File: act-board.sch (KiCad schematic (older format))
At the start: 15 parts, among them P1 B6B-PH-K-S(LF)(SN), P2 S2B-PH-K-S(LF)(SN), Q1 PN2222A, Q2 IRLB8721PBF, Q3 PN2222A, Q4 PN2222A

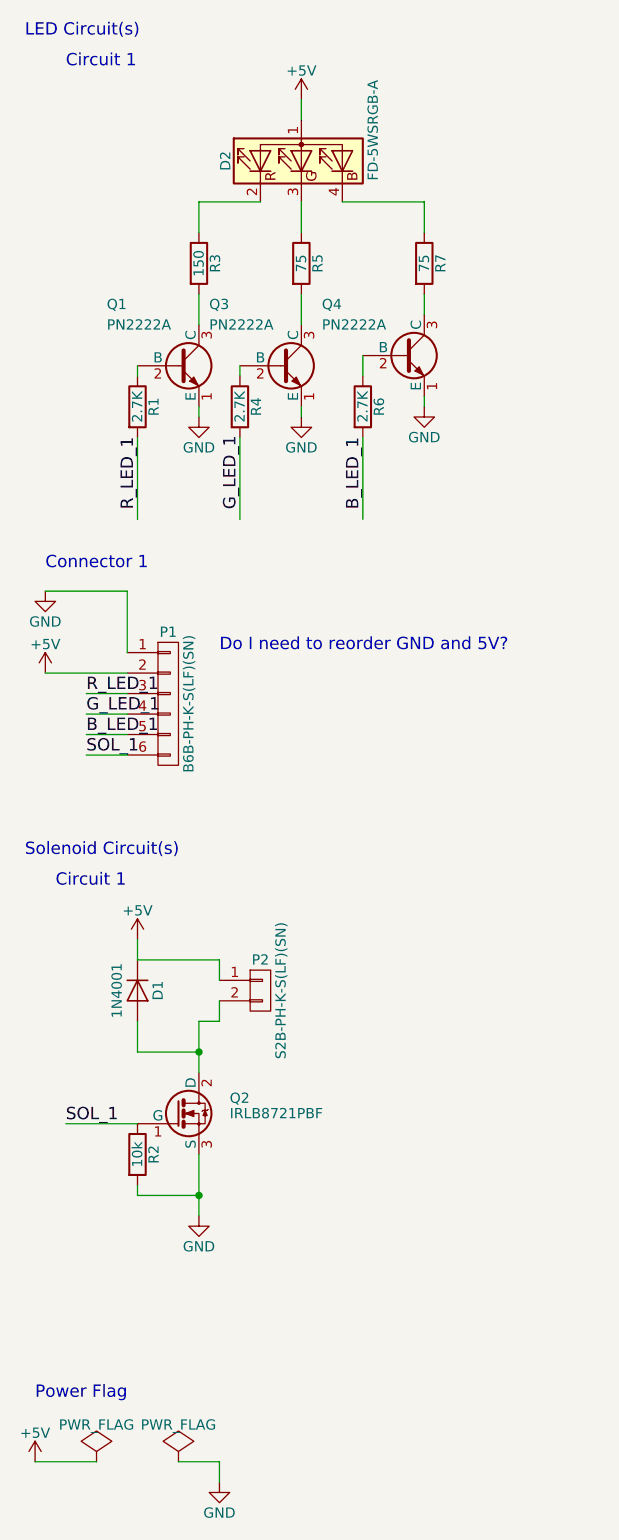
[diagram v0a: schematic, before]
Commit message: Fix RGB LED pad.
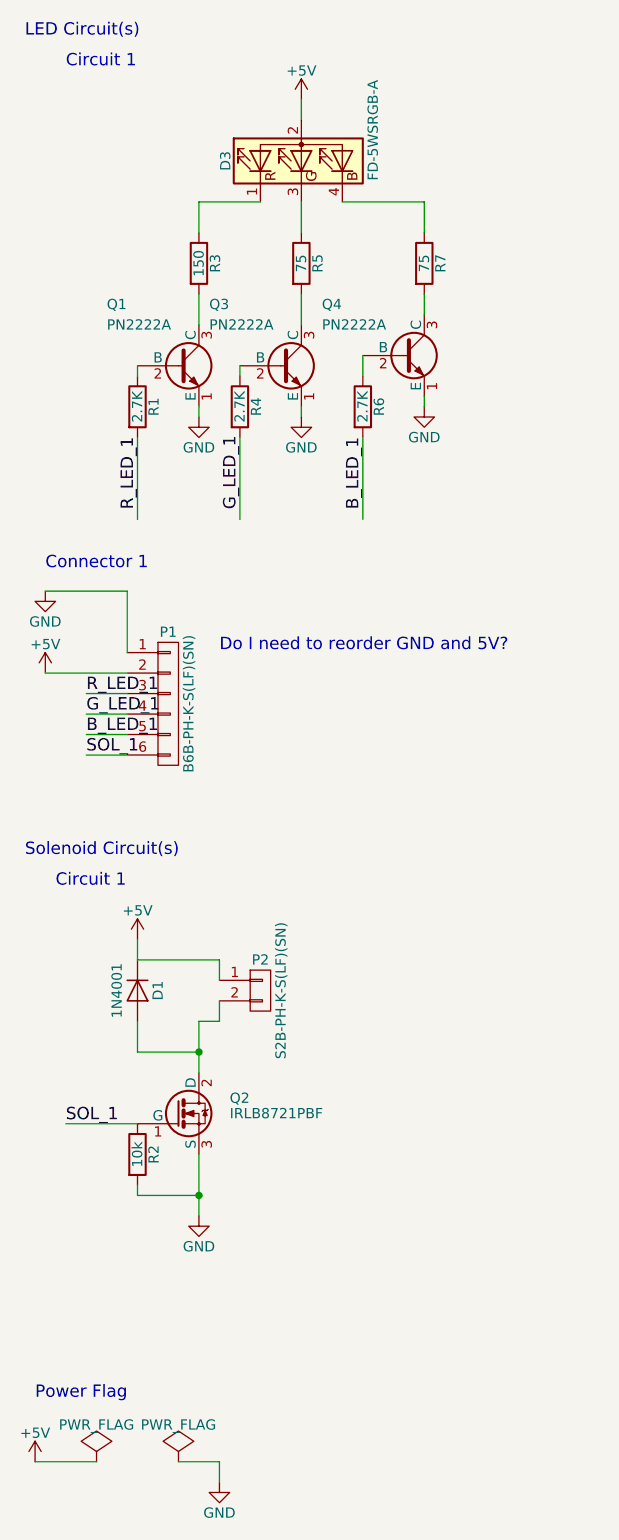
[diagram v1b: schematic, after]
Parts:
- removed D2: FD-5WSRGB-A, LEDs:LED-RGB-5MM_Common_Cathode, symbol LED_ARGB
- added D3: FD-5WSRGB-A, LEDs:LED_D5.0mm-4, symbol LED_RAGB
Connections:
- wire segments 40 -> 42
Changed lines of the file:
@@
 $EndDescr
-$Comp
-L LED_ARGB D2
-U 1 1 5865AF3E
-P 1900 1250
-F 0 "D2" H 1900 1620 50  0000 C CNN
-F 1 "FD-5WSRGB-A" H 2050 900 50  0000 C CNN
-F 2 "LEDs:LED-RGB-5MM_Common_Cathode" H 1900 1200 50  0001 C CNN
-F 3 "" H 1900 1200 50  0000 C CNN
-	1    1900 1250
-	0    -1   -1   0
-$EndComp
 $Comp
 L R R3
@@
 	1100 6300 1400 6300
 Wire Wire Line
-	1400 6100 1400 6400
+	1400 6100 1400 6300
+Wire Wire Line
+	1400 6300 1400 6400
 Wire Wire Line
 	1100 5150 1500 5150
@@
 	1100 5600 1400 5600
 Wire Wire Line
-	1400 5450 1400 5700
+	1400 5450 1400 5600
+Wire Wire Line
+	1400 5600 1400 5700
 Connection ~ 1400 5600
 Wire Wire Line
@@
 Text Notes 650  3250 0    60   ~ 0
 Connector 1
+$Comp
+L LED_RAGB D3
+U 1 1 58A093AD
+P 1900 1250
+F 0 "D3" H 1900 1620 50  0000 C CNN
+F 1 "FD-5WSRGB-A" H 2050 900 50  0000 C CNN
+F 2 "LEDs:LED_D5.0mm-4" H 1900 1200 50  0001 C CNN
+F 3 "" H 1900 1200 50  0000 C CNN
+	1    1900 1250
+	0    -1   -1   0
+$EndComp
 $EndSCHEMATC
